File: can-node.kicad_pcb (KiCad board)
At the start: 2 copper layers, 50 x 40 mm, 56 parts, among them P1 SWD, P2 DEBUG_UART, P3 CONN_01X03, P4 CONN_01X03, Q1 DMP6023LSS, SW1 SW_PUSH, SW2 SW_PUSH, SW3 SW_PUSH, U1 LMR16006, U2 SN74LVC1G08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

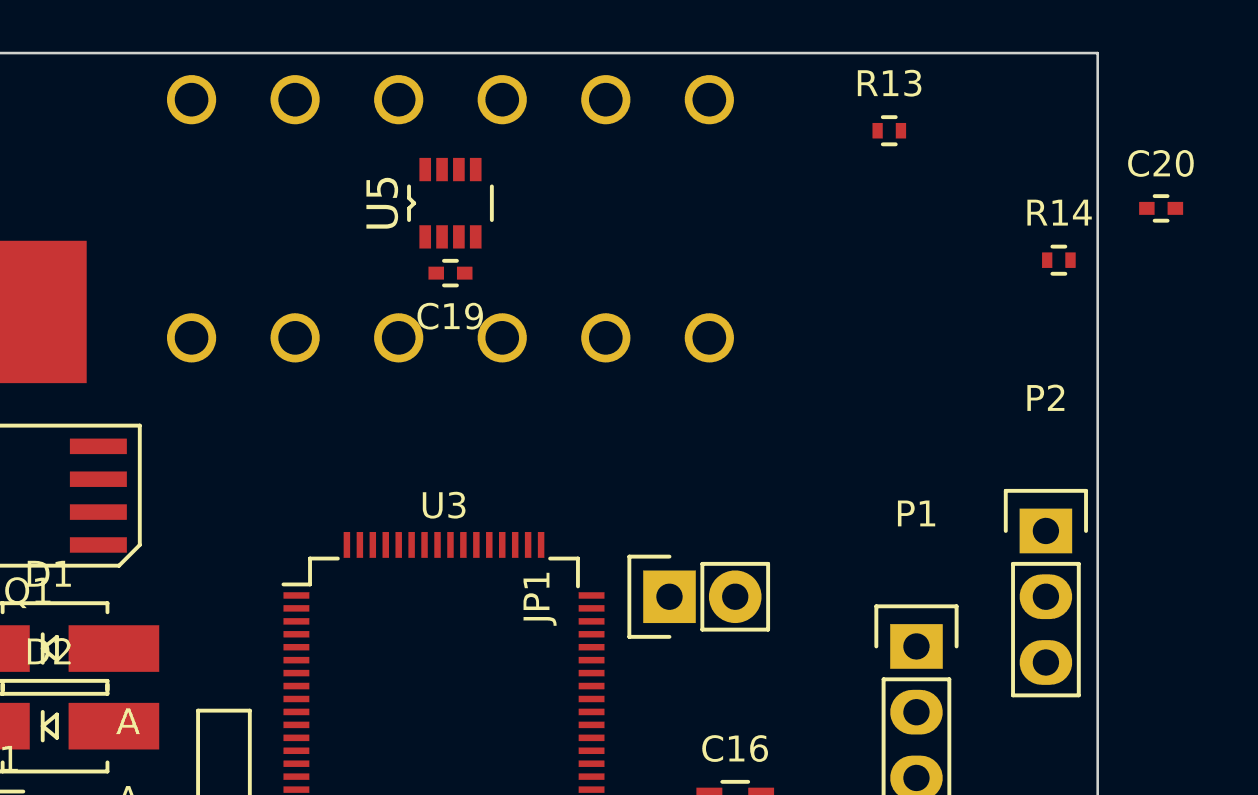
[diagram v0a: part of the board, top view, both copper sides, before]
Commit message: Use WAGO 218-106 connector
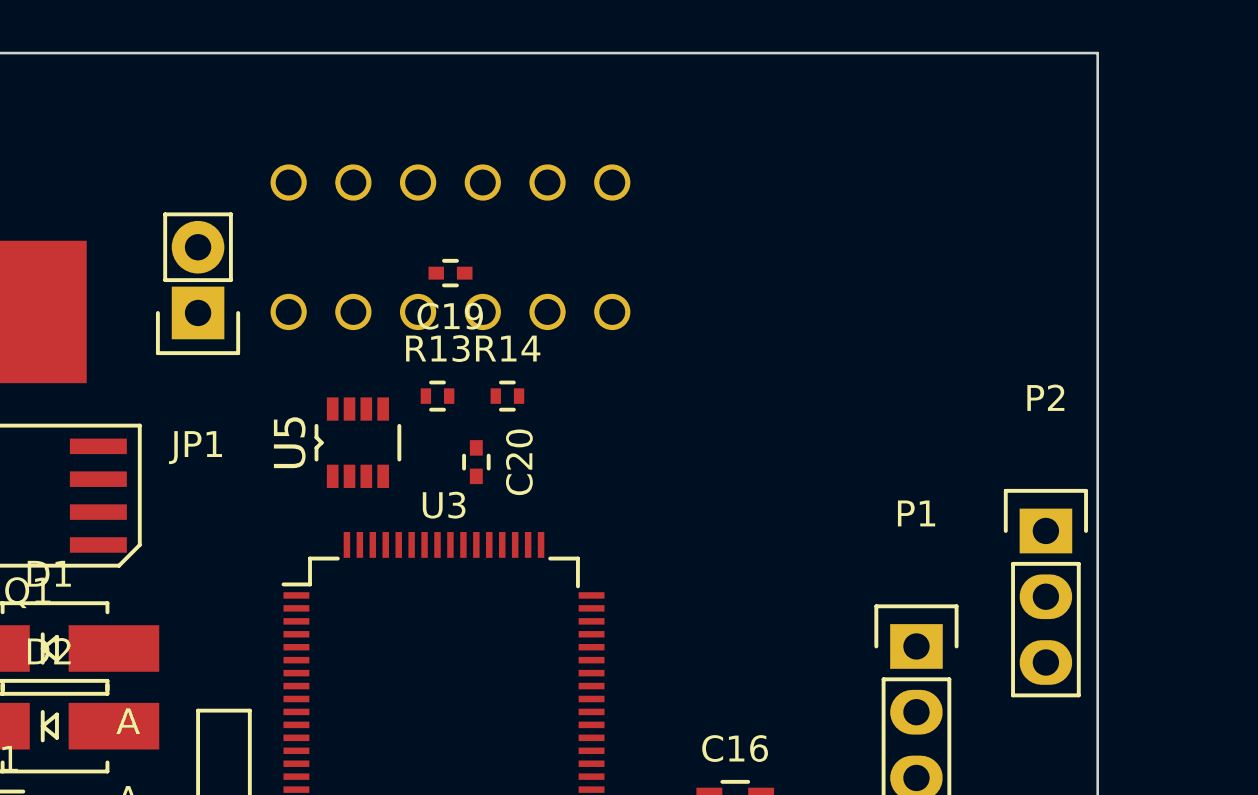
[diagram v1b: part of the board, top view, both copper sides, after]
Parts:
- removed P4: CONN_01X03, CAN_Node:WAGO_2060-1423
- P3: value CONN_01X03 -> CONN_01X06; footprint CAN_Node:WAGO_2060-1423 -> CAN_Node:WAGO_218-106
- moved C20 28.2 mm to (146.0, 95.8), turned to 270 degrees
- moved R14 21.9 mm to (147.2, 93.2)
- moved JP1 21.3 mm to (135.2, 90.0), turned to 180 degrees
- moved R13 20.2 mm to (144.5, 93.2)
- moved U5 9.92 mm to (141.4, 95.0)
- moved P3 6.10 mm to (145.0, 87.5), turned to 180 degrees

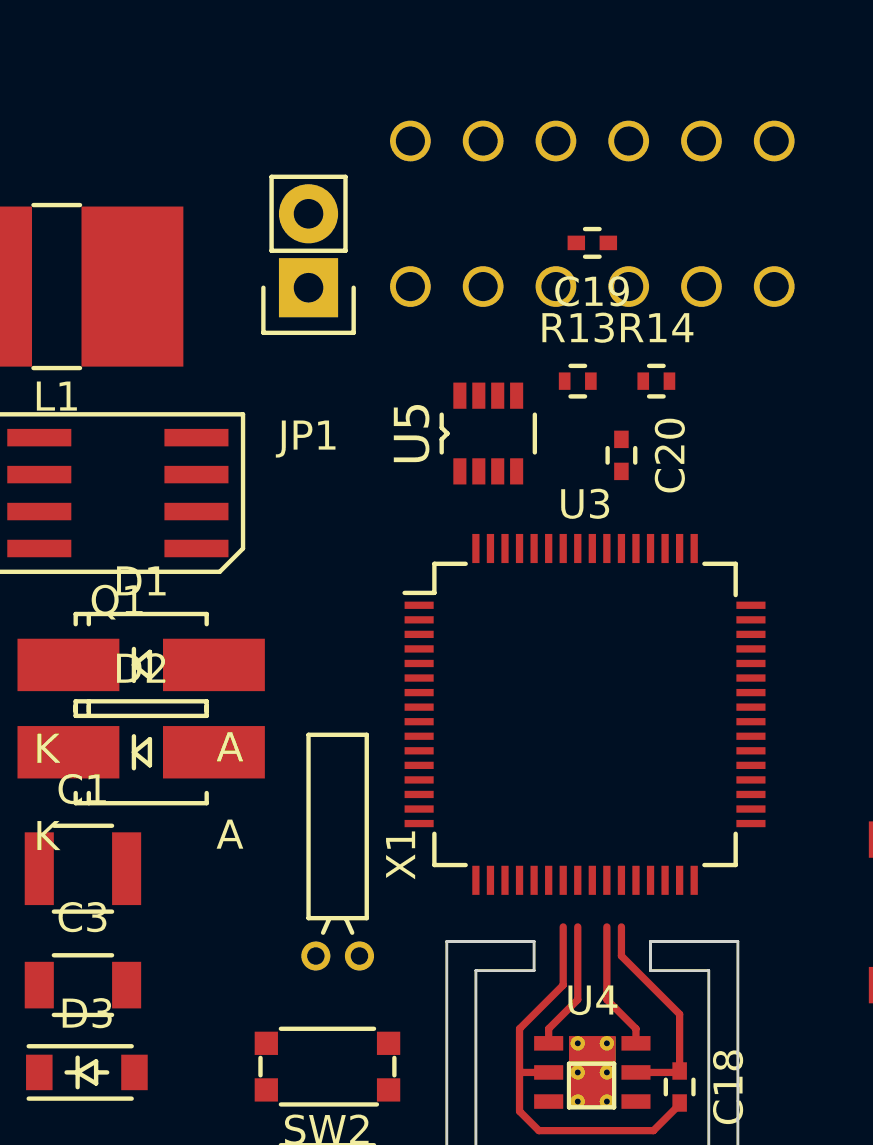
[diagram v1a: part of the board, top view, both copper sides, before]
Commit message: Use solder jumper for optional CAN termination, fix crystal symbol
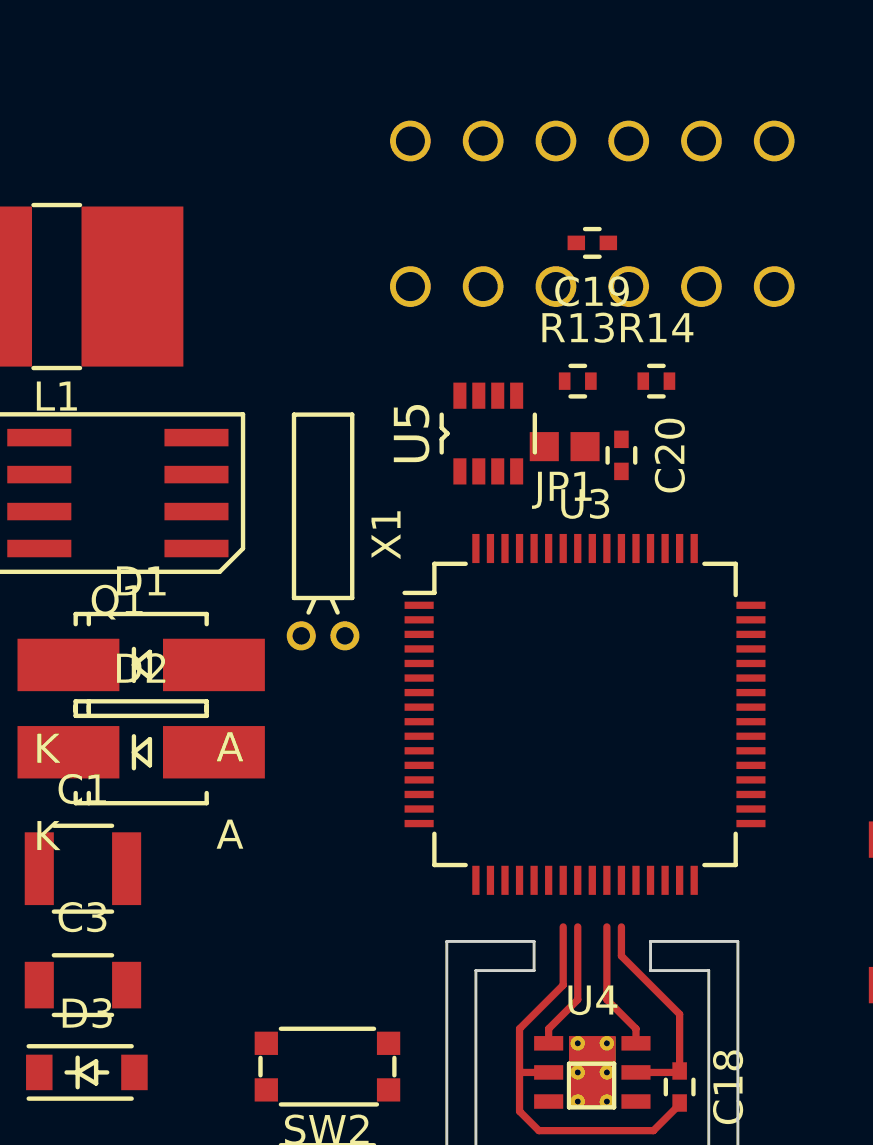
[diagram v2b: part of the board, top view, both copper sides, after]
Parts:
- JP1: footprint Pin_Headers:Pin_Header_Straight_1x02 -> CAN_Node:SolderJumper
- moved X1 11.0 mm to (135.8, 102.0)
- moved JP1 10.4 mm to (144.1, 95.5), turned to 0 degrees
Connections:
- X1 pad 2: (no net) -> Net-(C5-Pad1)
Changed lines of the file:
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@@
 (kicad_pcb (version 4) (host pcbnew 4.0.4+dfsg1-stable)
   (general
-    (links 136)
-    (no_connects 134)
+    (links 137)
+    (no_connects 135)
     (area 119.949999 79.949999 170.050001 120.050001)
     (thickness 1.6)
@@
     )
   )
-  (module Pin_Headers:Pin_Header_Straight_1x02 (layer F.Cu)
-    (at 135.25 90.04 180)
-    (descr "Through hole pin header")
-    (tags "pin header")
-    (fp_text reference JP1 (at 0 -5.1 180) (layer F.SilkS)
-      (effects (font (size 1 1) (thickness 0.15)))
-    )
-    (fp_text value Jumper_NC_Small (at 0 -3.1 180) (layer F.Fab)
-      (effects (font (size 1 1) (thickness 0.15)))
-    )
-    (fp_line (start 1.27 1.27) (end 1.27 3.81) (layer F.SilkS) (width 0.15))
-    (fp_line (start 1.55 -1.55) (end 1.55 0) (layer F.SilkS) (width 0.15))
-    (fp_line (start -1.75 -1.75) (end -1.75 4.3) (layer F.CrtYd) (width 0.05))
-    (fp_line (start 1.75 -1.75) (end 1.75 4.3) (layer F.CrtYd) (width 0.05))
-    (fp_line (start -1.75 -1.75) (end 1.75 -1.75) (layer F.CrtYd) (width 0.05))
-    (fp_line (start -1.75 4.3) (end 1.75 4.3) (layer F.CrtYd) (width 0.05))
-    (fp_line (start 1.27 1.27) (end -1.27 1.27) (layer F.SilkS) (width 0.15))
-    (fp_line (start -1.55 0) (end -1.55 -1.55) (layer F.SilkS) (width 0.15))
-    (fp_line (start -1.55 -1.55) (end 1.55 -1.55) (layer F.SilkS) (width 0.15))
-    (fp_line (start -1.27 1.27) (end -1.27 3.81) (layer F.SilkS) (width 0.15))
-    (fp_line (start -1.27 3.81) (end 1.27 3.81) (layer F.SilkS) (width 0.15))
-    (pad 1 thru_hole rect (at 0 0 180) (size 2.032 2.032) (drill 1.016) (layers *.Cu *.Mask F.SilkS)
-      (net 19 CANH_IN))
-    (pad 2 thru_hole oval (at 0 2.54 180) (size 2.032 2.032) (drill 1.016) (layers *.Cu *.Mask F.SilkS)
-      (net 20 "Net-(JP1-Pad2)"))
-    (model Pin_Headers.3dshapes/Pin_Header_Straight_1x02.wrl
-      (at (xyz 0 -0.05 0))
-      (scale (xyz 1 1 1))
-      (rotate (xyz 0 0 90))
-    )
-  )
   (module CAN_Node:SDE0604A_HandSoldering (layer F.Cu)
     (at 126.6 90)
@@
       (scale (xyz 0.394 0.394 0.394))
       (rotate (xyz 0 0 90))
-    )
-  )
-  (module CAN_Node:Crystal_DT-26 (layer F.Cu)
-    (at 136.2507 113)
-    (descr "Crystal, Quarz, Rundgehaeuse, round, horizontal, liegend, Uhrenquarz, Diam. 2mm,")
-    (tags "Crystal Quarz Rundgehaeuse round horizontal liegend Uhrenquarz Diam. 2mm")
-    (fp_text reference X1 (at 2.2 -3.5 270) (layer F.SilkS)
-      (effects (font (size 1 1) (thickness 0.15)))
-    )
-    (fp_text value "32.768KHz 12.5pF" (at 0 -2.7) (layer F.Fab)
-      (effects (font (size 1 1) (thickness 0.15)))
-    )
-    (fp_line (start -0.29972 -1.24968) (end -0.5 -0.8) (layer F.SilkS) (width 0.15))
-    (fp_line (start 0.29972 -1.24968) (end 0.5 -0.8) (layer F.SilkS) (width 0.15))
-    (fp_line (start 1 -1.3) (end 1 -7.6) (layer F.SilkS) (width 0.15))
-    (fp_line (start 1 -7.6) (end -1 -7.6) (layer F.SilkS) (width 0.15))
-    (fp_line (start -1 -7.6) (end -1 -1.3) (layer F.SilkS) (width 0.15))
-    (fp_line (start 1 -1.3) (end -1 -1.3) (layer F.SilkS) (width 0.15))
-    (pad 1 thru_hole circle (at -0.7493 0) (size 1.00076 1.00076) (drill 0.59944) (layers *.Cu *.Mask F.SilkS)
-      (net 6 "Net-(C4-Pad1)"))
-    (pad 2 thru_hole circle (at 0.7493 0) (size 1.00076 1.00076) (drill 0.59944) (layers *.Cu *.Mask F.SilkS))
-    (model ${KIPRJMOD}/lib/3d/crystal_DT-26.x3d
-      (at (xyz 0 0 0))
-      (scale (xyz 0.394 0.394 0.394))
-      (rotate (xyz -90 0 180))
     )
   )
@@
       (at (xyz 0 0 0))
       (scale (xyz 0.394 0.394 0.394))
+      (rotate (xyz -90 0 180))
+    )
+  )
+  (module CAN_Node:SolderJumper (layer F.Cu)
+    (at 144.05 95.5)
+    (fp_text reference JP1 (at 0 1.4) (layer F.SilkS)
+      (effects (font (size 1 1) (thickness 0.15)))
+    )
+    (fp_text value Jumper_NC_Small (at 0 -0.5) (layer F.Fab) hide
+      (effects (font (size 1 1) (thickness 0.15)))
+    )
+    (pad 1 smd rect (at -0.7 0) (size 1 1) (layers F.Cu F.Paste F.Mask)
+      (net 19 CANH_IN))
+    (pad 2 smd rect (at 0.7 0) (size 1 1) (layers F.Cu F.Paste F.Mask)
+      (net 20 "Net-(JP1-Pad2)"))
+  )
+  (module CAN_Node:Crystal_DT-26 (layer F.Cu)
+    (at 135.7507 102)
+    (descr "Crystal, Quarz, Rundgehaeuse, round, horizontal, liegend, Uhrenquarz, Diam. 2mm,")
+    (tags "Crystal Quarz Rundgehaeuse round horizontal liegend Uhrenquarz Diam. 2mm")
+    (fp_text reference X1 (at 2.2 -3.5 270) (layer F.SilkS)
+      (effects (font (size 1 1) (thickness 0.15)))
+    )
+    (fp_text value "32.768KHz 12.5pF" (at 0 -2.7) (layer F.Fab)
+      (effects (font (size 1 1) (thickness 0.15)))
+    )
+    (fp_line (start -0.29972 -1.24968) (end -0.5 -0.8) (layer F.SilkS) (width 0.15))
+    (fp_line (start 0.29972 -1.24968) (end 0.5 -0.8) (layer F.SilkS) (width 0.15))
+    (fp_line (start 1 -1.3) (end 1 -7.6) (layer F.SilkS) (width 0.15))
+    (fp_line (start 1 -7.6) (end -1 -7.6) (layer F.SilkS) (width 0.15))
+    (fp_line (start -1 -7.6) (end -1 -1.3) (layer F.SilkS) (width 0.15))
+    (fp_line (start 1 -1.3) (end -1 -1.3) (layer F.SilkS) (width 0.15))
+    (pad 1 thru_hole circle (at -0.7493 0) (size 1.00076 1.00076) (drill 0.59944) (layers *.Cu *.Mask F.SilkS)
+      (net 6 "Net-(C4-Pad1)"))
+    (pad 2 thru_hole circle (at 0.7493 0) (size 1.00076 1.00076) (drill 0.59944) (layers *.Cu *.Mask F.SilkS)
+      (net 7 "Net-(C5-Pad1)"))
+    (model ${KIPRJMOD}/lib/3d/crystal_DT-26.x3d
+      (at (xyz 0 0 0))
+      (scale (xyz 0.394 0.394 0.394))

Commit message: Layouting ...
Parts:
- removed JP1: Jumper_NC_Small, CAN_Node:SolderJumper
- SW1: moved to B.Cu
- moved R4 74.2 mm to (145.4, 68.0), turned to 180 degrees
- moved R2 69.9 mm to (141.0, 70.8), turned to 180 degrees
- moved U1 65.9 mm to (145.0, 72.2), turned to 90 degrees
- moved R3 65.3 mm to (148.0, 68.0), turned to 180 degrees
- moved R1 59.6 mm to (135.2, 77.8), turned to 270 degrees
- moved C13 53.9 mm to (152.0, 83.8), turned to 90 degrees
- moved C9 53.3 mm to (125.0, 103.0), turned to 270 degrees
- moved R9 53.2 mm to (162.7, 103.0)
- moved C14 52.5 mm to (154.0, 83.8), turned to 90 degrees
- moved C12 50.5 mm to (150.0, 83.8), turned to 90 degrees
- moved C3 44.6 mm to (154.5, 78.5), turned to 180 degrees
- moved D3 43.7 mm to (145.2, 77.0), turned to 270 degrees
- moved C2 43.6 mm to (147.8, 76.8), turned to 90 degrees
- moved R8 42.2 mm to (146.7, 107.5)
- moved C11 41.7 mm to (160.1, 89.0), turned to 180 degrees
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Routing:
- net GND: track 14.2 -> 17.3 mm
- added copper zone on F.Cu, net GND
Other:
- board size 50 x 40 mm -> 60 x 60 mm
- net class Power added: clearance 0.2, trace_width 0.5, via_dia 0.6, via_drill 0.4

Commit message: Layout: first version
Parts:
- added D6: LED_RGB_EP, CAN_Node:Everlight_19-337, F.Cu at (145.0, 110.0)
- added R15: 220, Resistors_SMD:R_0402, F.Cu at (140.0, 110.8)
- added R16: 220, Resistors_SMD:R_0402, F.Cu at (140.0, 112.2)
- added R17: 220, Resistors_SMD:R_0402, F.Cu at (140.0, 113.8)
- P3: value CONN_01X06 -> CONN_01X04; footprint CAN_Node:WAGO_218-106 -> CAN_Node:WAGO_218-104
- SW1: moved to F.Cu
- moved P1 48.1 mm to (122.5, 99.9)
- moved L1 28.7 mm to (126.2, 75.0), turned to 180 degrees
- moved D1 28.3 mm to (156.0, 75.5), turned to 270 degrees
- moved C14 27.2 mm to (141.2, 107.8), turned to 180 degrees
- moved C3 26.6 mm to (128.0, 81.2), turned to 0 degrees
- moved C13 24.3 mm to (147.8, 107.8), turned to 180 degrees
- moved R7 24.0 mm to (167.5, 116.5), turned to 90 degrees
- moved R1 22.9 mm to (156.0, 68.0)
- moved R9 22.1 mm to (155.0, 123.8)
- moved R14 21.9 mm to (144.5, 82.5), turned to 0 degrees
- moved R8 21.0 mm to (167.5, 110.2), turned to 90 degrees
- moved Q1 20.8 mm to (148.0, 75.0), turned to 270 degrees
- moved C20 19.4 mm to (142.5, 82.5), turned to 270 degrees
- moved D4 19.4 mm to (167.5, 113.8), turned to 90 degrees
- moved R3 19.0 mm to (132.8, 79.2), turned to 90 degrees
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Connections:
- net Net-(U3-Pad10) renamed /Microcontroller/PC2
- net Net-(U3-Pad11) renamed /Microcontroller/PC3
- net Net-(U3-Pad24) renamed /Microcontroller/PC4
- net Net-(U3-Pad25) renamed /Microcontroller/PC5
- net Net-(U3-Pad28) renamed /Microcontroller/PB2
- net Net-(U3-Pad37) renamed /Microcontroller/PC6
- net Net-(U3-Pad38) renamed /Microcontroller/PC7
- net Net-(U3-Pad57) renamed /Microcontroller/PB5
- net Net-(U3-Pad8) renamed /Microcontroller/PC0
- net Net-(U3-Pad9) renamed /Microcontroller/PC1
- C18 pad 1: Net-(C18-Pad1) -> +3.3VADC
- P2 pad 1: GND -> /Microcontroller/UART1_RX
- P2 pad 2: /Microcontroller/UART_RX -> /Microcontroller/UART1_TX
- P2 pad 3: /Microcontroller/UART_TX -> GND
- P3 pad 3: CANH_IN -> CANL_IN
- P3 pad 4: CANL_IN -> CANH_IN
- R10 pad 2: /Microcontroller/I2C1_SDA -> Net-(R10-Pad2)
- R11 pad 2: /Microcontroller/I2C1_SCL -> Net-(R11-Pad2)
- R13 pad 1: Net-(JP1-Pad2) -> CANH_IN
- U3 pad 16: /Microcontroller/UART_TX -> Net-(D6-Pad4)
- U3 pad 17: /Microcontroller/UART_RX -> Net-(U3-Pad17)
- U3 pad 26: Net-(D4-Pad2) -> /Microcontroller/PB0
- U3 pad 27: Net-(D5-Pad2) -> /Microcontroller/PB1
- U3 pad 29: Net-(U3-Pad29) -> Net-(R11-Pad2)
- U3 pad 30: Net-(U3-Pad30) -> Net-(R10-Pad2)
- U3 pad 33: Net-(U3-Pad33) -> Net-(C15-Pad1)
- U3 pad 34: Net-(U3-Pad34) -> Net-(C17-Pad1)
- U3 pad 35: Net-(U3-Pad35) -> Net-(D4-Pad2)
- U3 pad 36: Net-(U3-Pad36) -> Net-(D5-Pad2)
- U3 pad 42: Net-(U3-Pad42) -> /Microcontroller/UART1_TX
- U3 pad 43: Net-(U3-Pad43) -> /Microcontroller/UART1_RX
- U3 pad 51: Net-(U3-Pad51) -> CAN_STANDBY
- U3 pad 52: Net-(C15-Pad1) -> CAN_SHUTDOWN
- U3 pad 53: Net-(C17-Pad1) -> Net-(U3-Pad53)
- U3 pad 55: CAN_SHUTDOWN -> /Microcontroller/PB3
- U3 pad 56: CAN_STANDBY -> /Microcontroller/PB4
- U3 pad 58: /Microcontroller/I2C1_SCL -> /Microcontroller/PB6
- U3 pad 59: /Microcontroller/I2C1_SDA -> /Microcontroller/PB7
- U4 pad 1: /Microcontroller/I2C1_SDA -> Net-(R10-Pad2)
- U4 pad 5: Net-(C18-Pad1) -> +3.3VADC
- U4 pad 6: /Microcontroller/I2C1_SCL -> Net-(R11-Pad2)
- X1 pad 1: Net-(C4-Pad1) -> Net-(C5-Pad1)
- X1 pad 2: Net-(C5-Pad1) -> Net-(C4-Pad1)
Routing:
- net GND: track 17.3 -> 277.8 mm, vias 0 -> 27
- net +3.3VADC: track 0.00 -> 184.9 mm, vias 0 -> 5
- net (no net): track 0.00 -> 109.9 mm, vias 0 -> 16
- net /Microcontroller/SWCLK: track 0.00 -> 35.8 mm, vias 0 -> 1
- net /Microcontroller/UART1_RX: track 0.00 -> 32.1 mm, vias 0 -> 2
- net /Microcontroller/UART1_TX: track 0.00 -> 31.5 mm, vias 0 -> 2
- net /Microcontroller/SWDIO: track 0.00 -> 29.5 mm, vias 0 -> 1
- net Net-(C17-Pad1): track 0.00 -> 28.4 mm, vias 0 -> 2
- net Net-(R11-Pad2): track 0.00 -> 25.1 mm
- net Net-(C15-Pad1): track 0.00 -> 24.4 mm, vias 0 -> 2
- net Net-(D4-Pad2): track 0.00 -> 24.1 mm, vias 0 -> 2
- net Net-(R10-Pad2): track 0.00 -> 23.8 mm
- net Net-(D5-Pad2): track 0.00 -> 20.9 mm, vias 0 -> 2
- net Net-(R5-Pad2): track 0.00 -> 20.3 mm
- net Net-(C1-Pad1): track 0.00 -> 18.9 mm
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- added copper zone on B.Cu, net GND
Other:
- board size 60 x 60 mm -> 50 x 60 mm
